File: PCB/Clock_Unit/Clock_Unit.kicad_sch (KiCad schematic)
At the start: 10 parts, among them J1 Conn_01x04, J2 Conn_01x04, J3 Conn_01x04, J4 Conn_01x04

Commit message: Add center hole
m3 opening added
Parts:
- added H5: MountingHole, MountingHole:MountingHole_3.2mm_M3, symbol Mechanical:MountingHole
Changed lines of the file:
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@@
+	)
+	(symbol
+		(lib_id "Mechanical:MountingHole")
+		(at 247.65 41.91 0)
+		(unit 1)
+		(exclude_from_sim no)
+		(in_bom no)
+		(on_board yes)
+		(dnp no)
+		(fields_autoplaced yes)
+		(property "Reference" "H5"
+			(at 250.19 40.6399 0)
+			(effects
+				(font
+					(size 1.27 1.27)
+				)
+				(justify left)
+			)
+		)
+		(property "Value" "MountingHole"
+			(at 250.19 43.1799 0)
+			(effects
+				(font
+					(size 1.27 1.27)
+				)
+				(justify left)
+			)
+		)
+		(property "Footprint" "MountingHole:MountingHole_3.2mm_M3"
+			(at 247.65 41.91 0)
+			(effects
+				(font
+					(size 1.27 1.27)
+				)
+				(hide yes)
+			)
+		)
+		(property "Datasheet" "~"
+			(at 247.65 41.91 0)
+			(effects
+				(font
+					(size 1.27 1.27)
+				)
+				(hide yes)
+			)
+		)
+		(property "Description" "Mounting Hole without connection"
+			(at 247.65 41.91 0)
+			(effects
+				(font
+					(size 1.27 1.27)
+				)
+				(hide yes)
+			)
+		)
+		(instances
+			(project "Clock_Unit"
+				(path "/984dfde4-fced-41e6-9144-28eea2225a50"
+					(reference "H5")
+					(unit 1)
+				)
+			)
+		)
 	)
 	(symbol

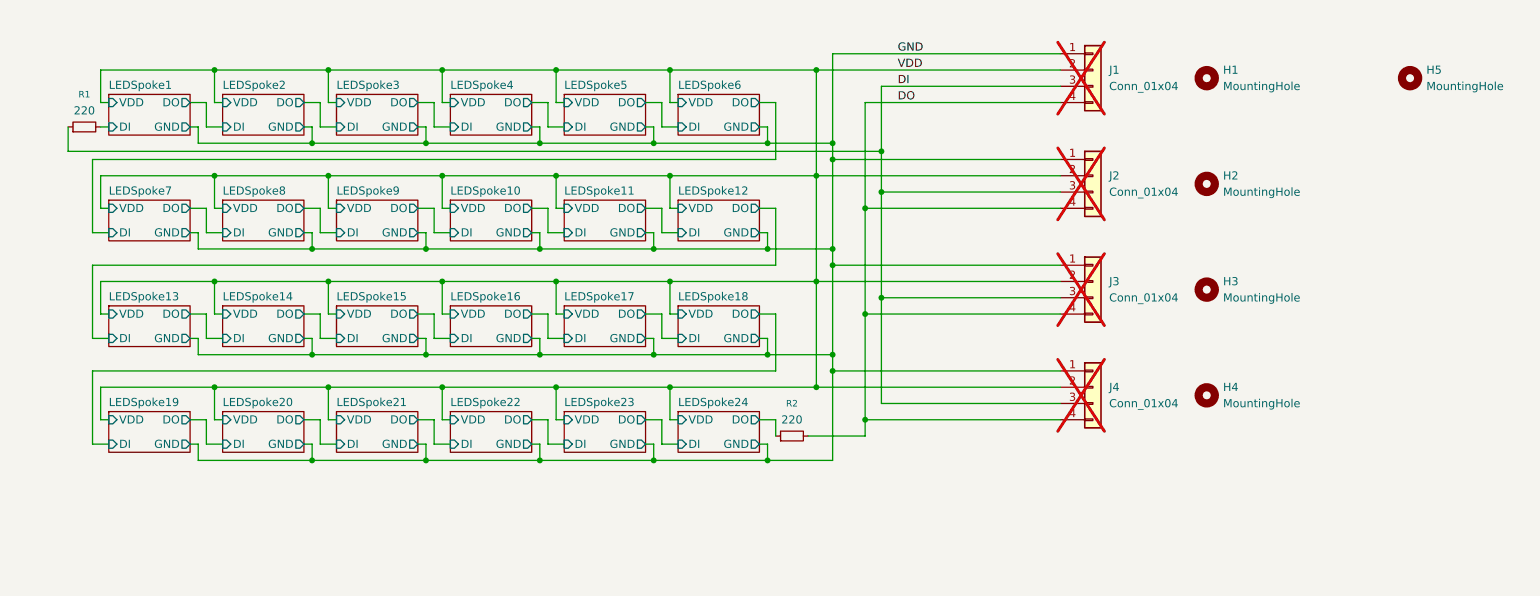
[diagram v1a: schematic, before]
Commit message: Schematic + PCB Updates
Corrected LED symbol and improved silkscreen
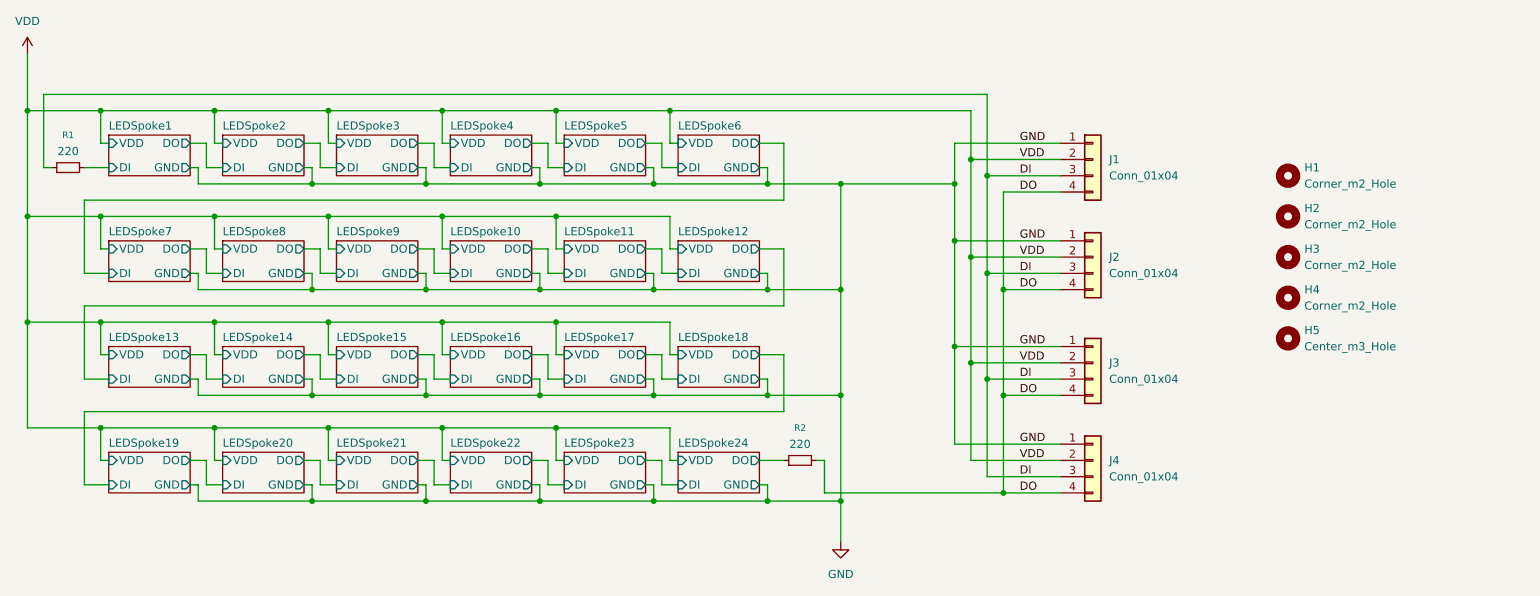
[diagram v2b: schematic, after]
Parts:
- H1, H2, H3, H4: value MountingHole -> Corner_m2_Hole
- H5: value MountingHole -> Center_m3_Hole
- J1, J2, J3, J4: now fitted
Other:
- moved on the sheet: H1, H2, H3, H4, H5, R1, R2
